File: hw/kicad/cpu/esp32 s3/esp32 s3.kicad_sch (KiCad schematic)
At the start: 40 parts, among them J1 TOP, J2 BUTTOM, J3 USB_B_Micro, SW1 SW_Push, U1 ESP32-S3-WROOM-1-N16R2, U2 ICM-42688-P

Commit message: 更新CPU板
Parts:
- added R19, R20: R, Resistor_SMD:R_0603_1608Metric, symbol Device:R
- R1, R29, R30: footprint Resistor_SMD:R_0805_2012Metric -> Resistor_SMD:R_0603_1608Metric
- R10, R11, R12, R13, R14, R15, R16, R17, R18, R21, R22, R23, R24, R25, R26, R27, R28, R3, R4, R5, R6, R7, R8, R9: value 100 -> R
- SW1: footprint Button_Switch_SMD:SW_DIP_SPSTx01_Slide_6.7x4.1mm_W6.73mm_P2.54mm_LowProfile_JPin -> Button_Switch_THT:SW_SPST_Omron_B3F-315x_Angled
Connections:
- net UART1_RX is gone; now on net UART1_Rx: R7.2
- net UART1_TX is gone; now on net UART1_Tx: R8.2
- net UART2_RX is gone; now on net UART2_Rx: R9.2
- net UART2_TX is gone; now on net UART2_Tx: R10.2
- net UART3_Rx is gone; now on net I2C_SDA: J1.9 (Pin_9), J2.10 (Pin_10)
- net UART3_Tx is gone; now on net I2C_CLK: J1.10 (Pin_10), J2.9 (Pin_9)
- net usb_d+ is gone; now on net usb+: U1.14 (IO20)
- net usb_d- is gone; now on net usb-: U1.13 (IO19)
- net GND: now also SW1.1; no longer R1.1
- net GPIO_1: now also J1.15 (Pin_15), J2.16 (Pin_16), R17.2; no longer J1.17 (Pin_17), J2.18 (Pin_18), R21.2
- net GPIO_10: now also J1.24 (Pin_24), J2.23 (Pin_23), R26.2; no longer J1.26 (Pin_26), J2.25 (Pin_25), R18.2
- net GPIO_2: now also J1.16 (Pin_16), J2.15 (Pin_15), R18.2; no longer J1.18 (Pin_18), J2.17 (Pin_17), R22.2
- net GPIO_3: now also J1.17 (Pin_17), J2.18 (Pin_18), R19.2; no longer J1.19 (Pin_19), J2.20 (Pin_20), R23.2
- net GPIO_4: now also J1.18 (Pin_18), J2.17 (Pin_17), R20.2; no longer J1.20 (Pin_20), J2.19 (Pin_19), R24.2
- net GPIO_5: now also J1.19 (Pin_19), J2.20 (Pin_20), R21.2; no longer J1.21 (Pin_21), J2.22 (Pin_22), R25.2
- net GPIO_6: now also J1.20 (Pin_20), J2.19 (Pin_19), R22.2; no longer J1.22 (Pin_22), J2.21 (Pin_21), R26.2
- net GPIO_7: now also J1.21 (Pin_21), J2.22 (Pin_22), R23.2; no longer J1.23 (Pin_23), J2.24 (Pin_24), R27.2
- net GPIO_8: now also J1.22 (Pin_22), J2.21 (Pin_21), R24.2; no longer J1.24 (Pin_24), J2.23 (Pin_23), R28.2
- net GPIO_9: now also J1.23 (Pin_23), J2.24 (Pin_24), R25.2; no longer J1.25 (Pin_25), J2.26 (Pin_26), R17.2
- net I2C_CLK: no longer J1.12 (Pin_12), J2.11 (Pin_11)
- net I2C_SDA: no longer J1.11 (Pin_11), J2.12 (Pin_12)
- net IMU_FSYNC: no longer U1.25 (IO48)
- net SPI_CLK: now also J1.12 (Pin_12), J2.11 (Pin_11); no longer J1.14 (Pin_14), J2.13 (Pin_13)
- net SPI_CS: now also J1.11 (Pin_11), J2.12 (Pin_12); no longer J1.13 (Pin_13), J2.14 (Pin_14)
- net SPI_MISO: now also J1.14 (Pin_14), J2.13 (Pin_13); no longer J1.16 (Pin_16), J2.15 (Pin_15)
- net SPI_MOSI: now also J1.13 (Pin_13), J2.14 (Pin_14); no longer J1.15 (Pin_15), J2.16 (Pin_16)
- net gpio1: now also R17.1, U1.25 (IO48); no longer R21.1, U1.28 (IO35)
- net gpio10: now also R26.1, U1.35 (IO42); no longer R18.1, U1.39 (IO1)
- net gpio2: now also R18.1, U1.26 (IO45); no longer R22.1, U1.29 (IO36)
- net gpio3: now also U1.28 (IO35), R19.1; no longer R23.1, U1.30 (IO37)
- net gpio4: now also U1.29 (IO36), R20.1; no longer R24.1, U1.31 (IO38)
- net gpio5: now also R21.1, U1.30 (IO37); no longer R25.1, R26.1, U1.32 (IO39), U1.33 (IO40)
- net gpio7: now also R23.1, U1.32 (IO39); no longer R27.1, U1.34 (IO41)
- net gpio8: now also R24.1, U1.33 (IO40); no longer R28.1, U1.35 (IO42)
- net gpio9: now also R25.1, U1.34 (IO41); no longer R17.1, U1.38 (IO2)
- net i2c_clk: now also R12.1, U1.20 (IO12); no longer R11.1, U1.10 (IO17)
- net i2c_sda: now also R11.1, U1.19 (IO11); no longer R12.1, U1.11 (IO18)
- net spi2_clk: now also U2.13 (AP_SCL/AP_SCLK); no longer U1.19 (IO11)
- net spi2_cs: now also U2.12 (AP_CS); no longer U1.17 (IO9)
- net spi2_miso: now also U2.1 (AP_SDO/AP_AD0); no longer U1.20 (IO12)
- net spi2_mosi: now also U2.14 (AP_SDA/AP_SDIO/AP_SDI); no longer U1.18 (IO10)
- net spi3_clk: no longer U2.13 (AP_SCL/AP_SCLK)
- net spi3_cs: no longer U2.12 (AP_CS)
- net spi3_miso: now also U1.23 (IO21); no longer U1.24 (IO47), U2.1 (AP_SDO/AP_AD0)
- net spi3_mosi: now also U1.24 (IO47); no longer U1.23 (IO21), U2.14 (AP_SDA/AP_SDIO/AP_SDI)
- net uart1_rx: now also U1.17 (IO9); no longer U1.9 (IO16)
- net uart1_tx: now also U1.18 (IO10); no longer U1.8 (IO15)
- net at U1.27 (IO0): now also R1.2; no longer SW1.2
- net USB+ renamed usb+
- net USB- renamed usb-
- new net: R1.1, SW1.2
- new net GPIO_11: J1.25 (Pin_25), J2.26 (Pin_26), R27.2
- new net GPIO_12: J1.26 (Pin_26), J2.25 (Pin_25), R28.2
- new net gpio11: R27.1, U1.38 (IO2)
- new net gpio12: R28.1, U1.39 (IO1)
- new net gpio6: R22.1, U1.31 (IO38)
- no-connect marks 5 -> 2
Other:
- note added: "烧录固件时，长按sw1调用esp_restart重启至boot模式，刚好io0此时也拉低"
- moved on the sheet: R1, SW1, U1

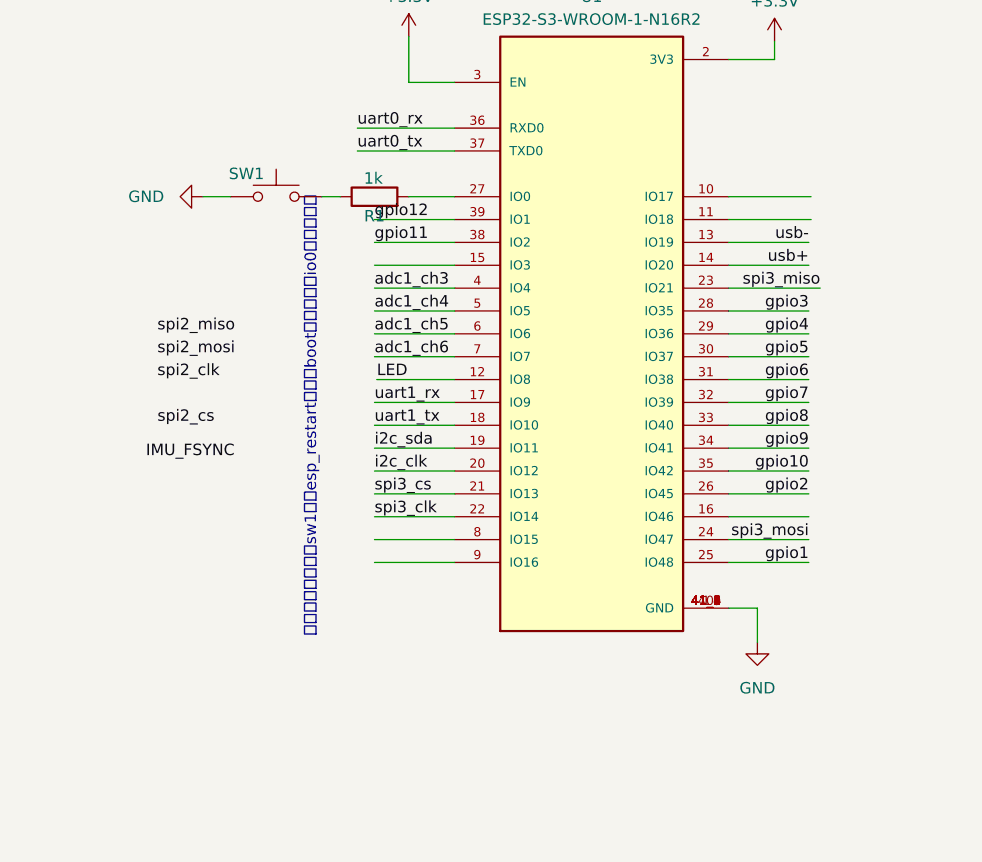
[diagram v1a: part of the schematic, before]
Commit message: 更新ESP32 S3 CPU板
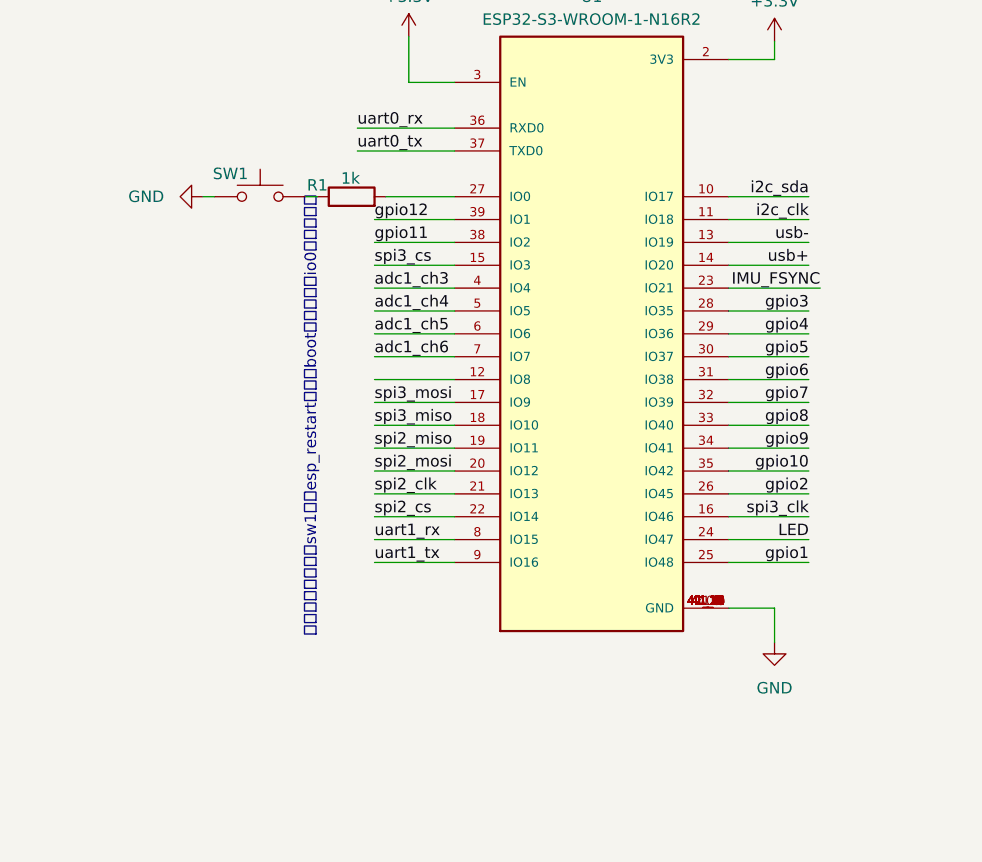
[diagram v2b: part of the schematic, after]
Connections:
- net GND: now also U1.41_10 (GND), U1.41_11 (GND), U1.41_12 (GND), U1.41_13 (GND), U1.41_14 (GND), U1.41_15 (GND), U1.41_16 (GND), U1.41_17 (GND), U1.41_18 (GND), U1.41_19 (GND), U1.41_20 (GND), U1.41_21 (GND)
- net IMU_FSYNC: now also U1.23 (IO21)
- net LED: now also U1.24 (IO47); no longer U1.12 (IO8)
- net i2c_clk: now also U1.11 (IO18); no longer U1.20 (IO12)
- net i2c_sda: now also U1.10 (IO17); no longer U1.19 (IO11)
- net spi2_clk: now also U1.21 (IO13)
- net spi2_cs: now also U1.22 (IO14)
- net spi2_miso: now also U1.19 (IO11)
- net spi2_mosi: now also U1.20 (IO12)
- net spi3_clk: now also U1.16 (IO46); no longer U1.22 (IO14)
- net spi3_cs: now also U1.15 (IO3); no longer U1.21 (IO13)
- net spi3_miso: now also U1.18 (IO10); no longer U1.23 (IO21)
- net spi3_mosi: now also U1.17 (IO9); no longer U1.24 (IO47)
- net uart1_rx: now also U1.8 (IO15); no longer U1.17 (IO9)
- net uart1_tx: now also U1.9 (IO16); no longer U1.18 (IO10)
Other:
- moved on the sheet: R1, SW1
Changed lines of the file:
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@@
     (stroke (width 0) (type default))
   )
-  (wire (pts (xy 63.754 142.24) (xy 72.39 142.24))
+  (wire (pts (xy 63.5 142.24) (xy 72.39 142.24))
     (stroke (width 0) (type default))
   )
@@
     (stroke (width 0) (type default))
   )
-  (wire (pts (xy 106.045 167.64) (xy 106.045 171.45))
-    (stroke (width 0) (type default))
-  )
   (wire (pts (xy 275.59 77.47) (xy 266.7 77.47))
     (stroke (width 0) (type default))
@@
     (stroke (width 0) (type default))
   )
-  (wire (pts (xy 112.014 121.92) (xy 102.87 121.92))
+  (wire (pts (xy 111.76 121.92) (xy 102.87 121.92))
     (stroke (width 0) (type default))
   )
@@
     (stroke (width 0) (type default))
   )
-  (wire (pts (xy 57.658 121.92) (xy 59.69 121.92))
+  (wire (pts (xy 55.88 121.92) (xy 57.15 121.92))
     (stroke (width 0) (type default))
   )
@@
     (stroke (width 0) (type default))
   )
-  (wire (pts (xy 44.45 121.92) (xy 47.498 121.92))
+  (wire (pts (xy 44.45 121.92) (xy 45.72 121.92))
     (stroke (width 0) (type default))
   )
@@
     (stroke (width 0) (type default))
   )
+  (wire (pts (xy 107.95 167.64) (xy 107.95 171.45))
+    (stroke (width 0) (type default))
+  )
   (wire (pts (xy 275.59 69.85) (xy 266.7 69.85))
     (stroke (width 0) (type default))
@@
     (stroke (width 0) (type default))
   )
-  (wire (pts (xy 67.31 121.92) (xy 72.39 121.92))
+  (wire (pts (xy 64.77 121.92) (xy 72.39 121.92))
     (stroke (width 0) (type default))
   )
@@
     (stroke (width 0) (type default))
   )
-  (wire (pts (xy 112.014 124.46) (xy 102.87 124.46))
+  (wire (pts (xy 111.76 124.46) (xy 102.87 124.46))
     (stroke (width 0) (type default))
   )
@@
     (stroke (width 0) (type default))
   )
-  (wire (pts (xy 102.87 167.64) (xy 106.045 167.64))
+  (wire (pts (xy 102.87 167.64) (xy 107.95 167.64))
     (stroke (width 0) (type default))
   )
@@
     (effects (font (size 1.27 1.27)) (justify right bottom))
   )
-  (label "IMU_FSYNC" (at 38.1 151.13 0) (fields_autoplaced)
-    (effects (font (size 1.27 1.27)) (justify left bottom))
-  )
-  (label "spi3_mosi" (at 111.76 160.02 180) (fields_autoplaced)
-    (effects (font (size 1.27 1.27)) (justify right bottom))
+  (label "IMU_FSYNC" (at 113.03 132.08 180) (fields_autoplaced)
+    (effects (font (size 1.27 1.27)) (justify right bottom))
+  )
+  (label "spi3_mosi" (at 63.5 144.78 0) (fields_autoplaced)
+    (effects (font (size 1.27 1.27)) (justify left bottom))
   )
   (label "adc1_ch4" (at 149.86 27.94 0) (fields_autoplaced)
@@
     (effects (font (size 1.27 1.27)) (justify left bottom))
   )
-  (label "spi3_clk" (at 63.5 157.48 0) (fields_autoplaced)
-    (effects (font (size 1.27 1.27)) (justify left bottom))
+  (label "spi3_clk" (at 111.76 157.48 180) (fields_autoplaced)
+    (effects (font (size 1.27 1.27)) (justify right bottom))
   )
   (label "LED" (at 107.315 50.8 0) (fields_autoplaced)
@@
     (effects (font (size 1.27 1.27)) (justify left bottom))
   )
-  (label "uart1_tx" (at 63.5 147.32 0) (fields_autoplaced)
+  (label "uart1_tx" (at 63.5 162.56 0) (fields_autoplaced)
     (effects (font (size 1.27 1.27)) (justify left bottom))
   )
@@
     (effects (font (size 1.27 1.27)) (justify right bottom))
   )
-  (label "uart1_rx" (at 63.5 144.78 0) (fields_autoplaced)
+  (label "uart1_rx" (at 63.5 160.02 0) (fields_autoplaced)
     (effects (font (size 1.27 1.27)) (justify left bottom))
   )
@@
     (effects (font (size 1.27 1.27)) (justify left bottom))
   )
-  (label "spi2_cs" (at 45.72 147.32 180) (fields_autoplaced)
-    (effects (font (size 1.27 1.27)) (justify right bottom))
+  (label "spi2_cs" (at 63.5 157.48 0) (fields_autoplaced)
+    (effects (font (size 1.27 1.27)) (justify left bottom))
   )
   (label "GPIO_2" (at 185.42 74.93 180) (fields_autoplaced)
@@
     (effects (font (size 1.27 1.27)) (justify left bottom))
   )
-  (label "spi3_miso" (at 113.03 132.08 180) (fields_autoplaced)
-    (effects (font (size 1.27 1.27)) (justify right bottom))
+  (label "spi3_miso" (at 63.5 147.32 0) (fields_autoplaced)
+    (effects (font (size 1.27 1.27)) (justify left bottom))
   )
   (label "GPIO_11" (at 185.42 102.87 180) (fields_autoplaced)
@@
     (effects (font (size 1.27 1.27)) (justify right bottom))
   )
-  (label "i2c_sda" (at 63.5 149.86 0) (fields_autoplaced)
-    (effects (font (size 1.27 1.27)) (justify left bottom))
+  (label "i2c_sda" (at 111.76 121.92 180) (fields_autoplaced)
+    (effects (font (size 1.27 1.27)) (justify right bottom))
   )
   (label "ADC_2" (at 184.15 27.94 180) (fields_autoplaced)
@@
     (effects (font (size 1.27 1.27)) (justify right bottom))
   )
-  (label "spi2_miso" (at 39.37 137.16 0) (fields_autoplaced)
+  (label "spi2_miso" (at 63.5 149.86 0) (fields_autoplaced)
     (effects (font (size 1.27 1.27)) (justify left bottom))
   )
@@
     (effects (font (size 1.27 1.27)) (justify right bottom))
   )
-  (label "spi3_cs" (at 63.5 154.94 0) (fields_autoplaced)
+  (label "spi3_cs" (at 63.5 129.54 0) (fields_autoplaced)
     (effects (font (size 1.27 1.27)) (justify left bottom))
   )
@@
     (effects (font (size 1.27 1.27)) (justify left bottom))
   )
-  (label "LED" (at 63.754 142.24 0) (fields_autoplaced)
-    (effects (font (size 1.27 1.27)) (justify left bottom))
+  (label "LED" (at 111.76 160.02 180) (fields_autoplaced)
+    (effects (font (size 1.27 1.27)) (justify right bottom))
   )
   (label "UART1_Tx" (at 238.76 34.29 180) (fields_autoplaced)
@@
     (effects (font (size 1.27 1.27)) (justify right bottom))
   )
-  (label "spi2_clk" (at 39.37 142.24 0) (fields_autoplaced)
+  (label "spi2_clk" (at 63.5 154.94 0) (fields_autoplaced)
     (effects (font (size 1.27 1.27)) (justify left bottom))
   )
@@
     (effects (font (size 1.27 1.27)) (justify left bottom))
   )
-  (label "i2c_clk" (at 63.5 152.4 0) (fields_autoplaced)
-    (effects (font (size 1.27 1.27)) (justify left bottom))
+  (label "i2c_clk" (at 111.76 124.46 180) (fields_autoplaced)
+    (effects (font (size 1.27 1.27)) (justify right bottom))
   )
   (label "SPI_CLK" (at 275.59 41.91 180) (fields_autoplaced)
@@
     (effects (font (size 1.27 1.27)) (justify left bottom))
   )
-  (label "spi2_mosi" (at 39.37 139.7 0) (fields_autoplaced)
+  (label "spi2_mosi" (at 63.5 152.4 0) (fields_autoplaced)
     (effects (font (size 1.27 1.27)) (justify left bottom))
   )
@@
     (pin "8")
     (pin "9")
+    (pin "41_10")
+    (pin "41_11")
+    (pin "41_12")
+    (pin "41_13")
+    (pin "41_14")
+    (pin "41_15")
+    (pin "41_16")
+    (pin "41_17")
+    (pin "41_18")
+    (pin "41_19")
+    (pin "41_20")
+    (pin "41_21")
     (instances
       (project "esp32 s3"
@@
     )
   )
-  (symbol (lib_id "Switch:SW_Push") (at 52.578 121.92 0) (unit 1)
+  (symbol (lib_id "Switch:SW_Push") (at 50.8 121.92 0) (unit 1)
     (in_bom yes) (on_board yes) (dnp no)
-    (property "Reference" "SW1" (at 49.276 119.38 0)
+    (property "Reference" "SW1" (at 47.498 119.38 0)
       (effects (font (size 1.27 1.27)))
     )
-    (property "Value" "SW_Push" (at 52.578 116.84 0)
-      (effects (font (size 1.27 1.27)) hide)
-    )
-    (property "Footprint" "Button_Switch_THT:SW_SPST_Omron_B3F-315x_Angled" (at 52.578 116.84 0)
-      (effects (font (size 1.27 1.27)) hide)
-    )
-    (property "Datasheet" "~" (at 52.578 116.84 0)
+    (property "Value" "SW_Push" (at 50.8 116.84 0)
+      (effects (font (size 1.27 1.27)) hide)
+    )
+    (property "Footprint" "Button_Switch_THT:SW_SPST_Omron_B3F-315x_Angled" (at 50.8 116.84 0)
+      (effects (font (size 1.27 1.27)) hide)
+    )
+    (property "Datasheet" "~" (at 50.8 116.84 0)
       (effects (font (size 1.27 1.27)) hide)
     )
@@
     )
   )
-  (symbol (lib_id "power:GND") (at 106.045 171.45 0) (unit 1)
-    (in_bom yes) (on_board yes) (dnp no) (fields_autoplaced)
-    (property "Reference" "#PWR05" (at 106.045 177.8 0)
-      (effects (font (size 1.27 1.27)) hide)
-    )
-    (property "Value" "GND" (at 106.045 176.53 0)
+  (symbol (lib_id "power:GND") (at 107.95 171.45 0) (mirror y) (unit 1)
+    (in_bom yes) (on_board yes) (dnp no) (fields_autoplaced)
+    (property "Reference" "#PWR05" (at 107.95 177.8 0)
+      (effects (font (size 1.27 1.27)) hide)
+    )
+    (property "Value" "GND" (at 107.95 176.53 0)
       (effects (font (size 1.27 1.27)))
     )
-    (property "Footprint" "" (at 106.045 171.45 0)
-      (effects (font (size 1.27 1.27)) hide)
-    )
-    (property "Datasheet" "" (at 106.045 171.45 0)
+    (property "Footprint" "" (at 107.95 171.45 0)
+      (effects (font (size 1.27 1.27)) hide)
+    )
+    (property "Datasheet" "" (at 107.95 171.45 0)
       (effects (font (size 1.27 1.27)) hide)
     )
@@
     )
   )
-  (symbol (lib_id "Device:R") (at 63.5 121.92 90) (unit 1)
+  (symbol (lib_id "Device:R") (at 60.96 121.92 90) (unit 1)
     (in_bom yes) (on_board yes) (dnp no)
-    (property "Reference" "R1" (at 63.5 124.079 90)
+    (property "Reference" "R1" (at 57.15 120.65 90)
       (effects (font (size 1.27 1.27)))
     )
-    (property "Value" "1k" (at 63.373 119.888 90)
+    (property "Value" "1k" (at 60.833 119.888 90)
       (effects (font (size 1.27 1.27)))
     )
-    (property "Footprint" "Resistor_SMD:R_0603_1608Metric" (at 63.5 123.698 90)
-      (effects (font (size 1.27 1.27)) hide)
-    )
-    (property "Datasheet" "~" (at 63.5 121.92 0)
-      (effects (font (size 1.27 1.27)) hide)
-    )
+    (property "Footprint" "Resistor_SMD:R_0603_1608Metric" (at 60.96 123.698 90)
+      (effects (font (size 1.27 1.27)) hide)
+    )
+    (property "Datasheet" "~" (at 60.96 121.92 0)
+      (effects (font (size 1.27 1.27)) hide)
+    )
